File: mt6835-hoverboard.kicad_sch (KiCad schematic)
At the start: 4 parts, among them U1 MT6835

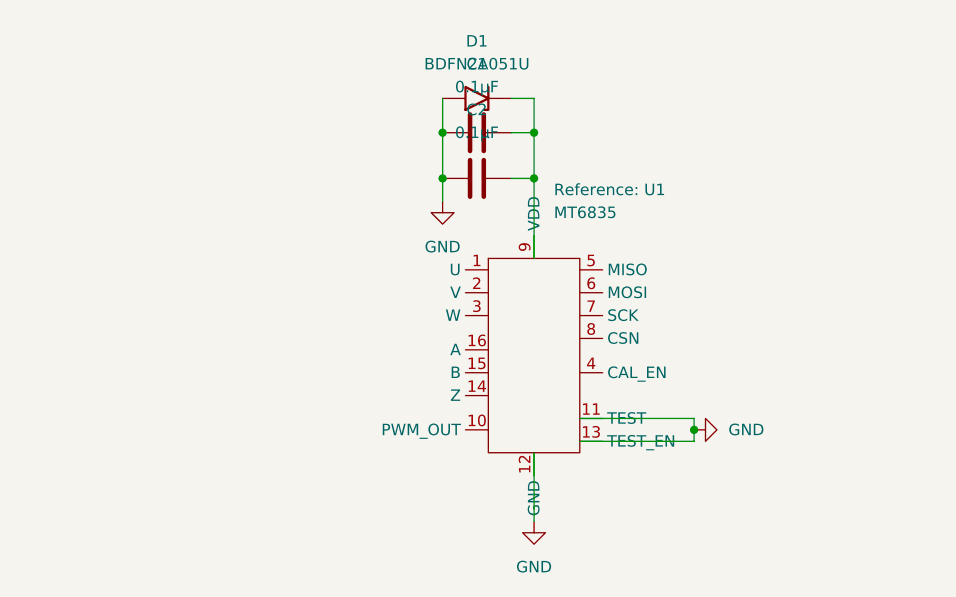
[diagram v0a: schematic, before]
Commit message: update schematic
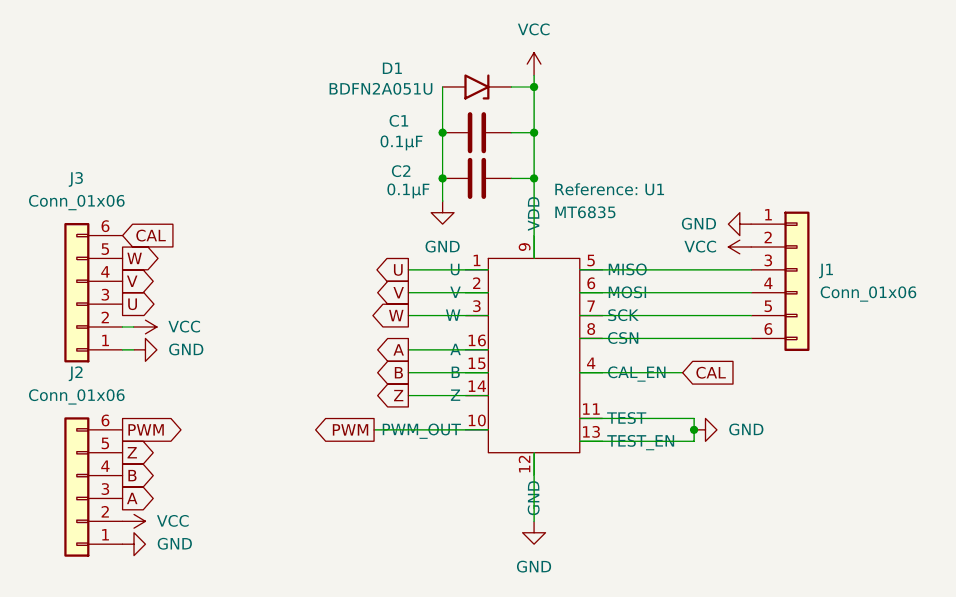
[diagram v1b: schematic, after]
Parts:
- added J1, J2, J3: Conn_01x06, symbol Connector_Generic:Conn_01x06
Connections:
- net GND: now also J1.1 (Pin_1), J2.1 (Pin_1), J3.1 (Pin_1)
- net VCC: now reaches C1.2, C2.2, D1.1 (A1), U1.9 (VDD)
- net VCC: now also J1.2 (Pin_2), J2.2 (Pin_2), J3.2 (Pin_2)
- net U: now reaches U1.1 (U)
- net U: now also J3.3 (Pin_3)
- net PWM: now reaches U1.10 (PWM_OUT)
- net PWM: now also J2.6 (Pin_6)
- net Z: now reaches U1.14 (Z)
- net Z: now also J2.5 (Pin_5)
- net B: now reaches U1.15 (B)
- net B: now also J2.4 (Pin_4)
- net A: now reaches U1.16 (A)
- net A: now also J2.3 (Pin_3)
- net V: now reaches U1.2 (V)
- net V: now also J3.4 (Pin_4)
- net W: now reaches U1.3 (W)
- net W: now also J3.5 (Pin_5)
- net CAL: now reaches U1.4 (CAL_EN)
- net CAL: now also J3.6 (Pin_6)
- net at U1.5 (MISO): now also J1.3 (Pin_3)
- net at U1.6 (MOSI): now also J1.4 (Pin_4)
- net at U1.7 (SCK): now also J1.5 (Pin_5)
- net at U1.8 (CSN): now also J1.6 (Pin_6)
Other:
- moved on the sheet: D1

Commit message: Revision 1.1: Good for production
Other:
- company: (none) -> mcells
- title: (none) -> MT6835 Breakout (eg. for Hoverboard Motors)
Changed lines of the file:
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@@
 	(generator_version "8.0")
 	(paper "A4")
+	(title_block
+		(title "MT6835 Breakout (eg. for Hoverboard Motors)")
+		(date "2024-07-08")
+		(rev "1.1")
+		(company "mcells")
+	)
 	(junction
 		(at 127 77.47)
